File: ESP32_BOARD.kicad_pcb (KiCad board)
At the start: 4 copper layers, 36 x 63 mm, 70 parts, among them IC1 AP2112K-3.3, IC2 MPQ4420HGJ-Z, IC3 W25Q128JVSIQ, IC4 ESP32-S3R8, IC5 AW9364DNR, Q1 40MHz, SW1 TS-1010B-B-A, SW2 PTS810SJK250SMTRLFS, SW3 PTS810SJK250SMTRLFS

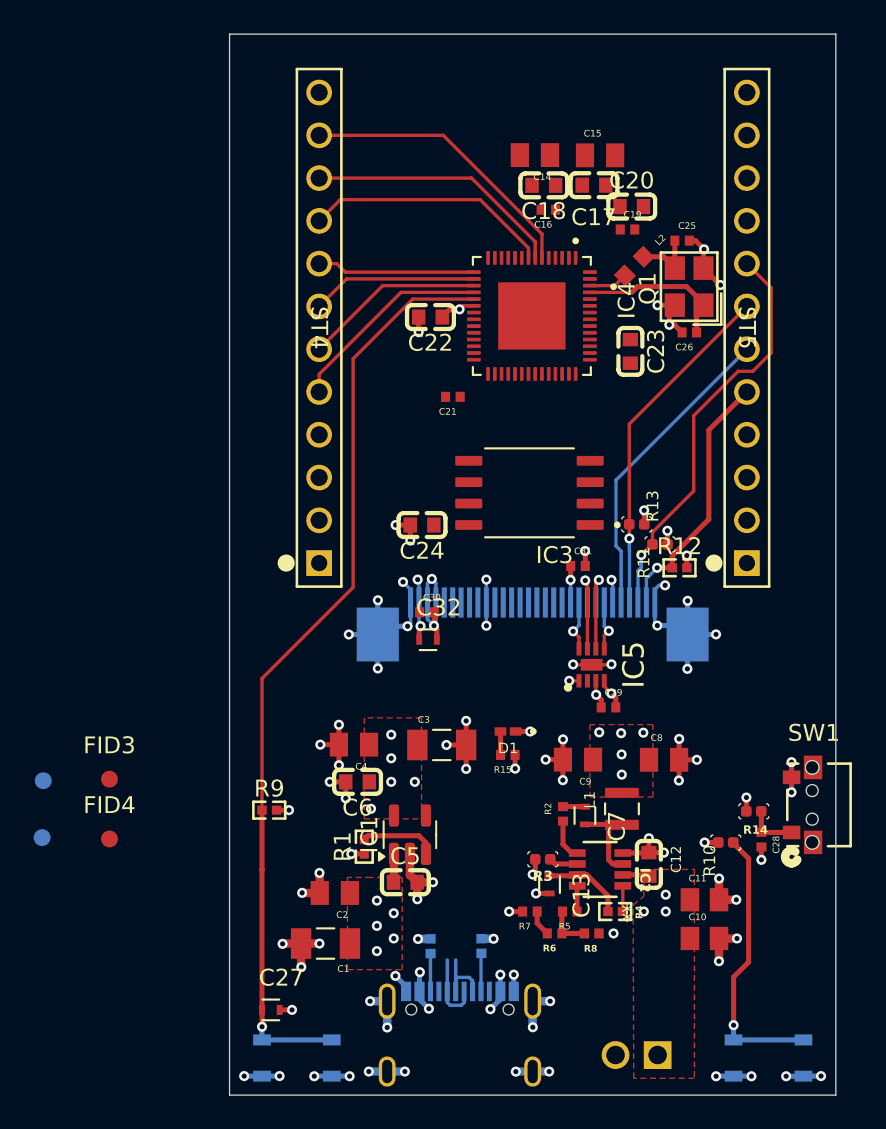
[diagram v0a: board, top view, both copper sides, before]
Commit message: Routing done | First Iteration
Silkscreen of components kinda done
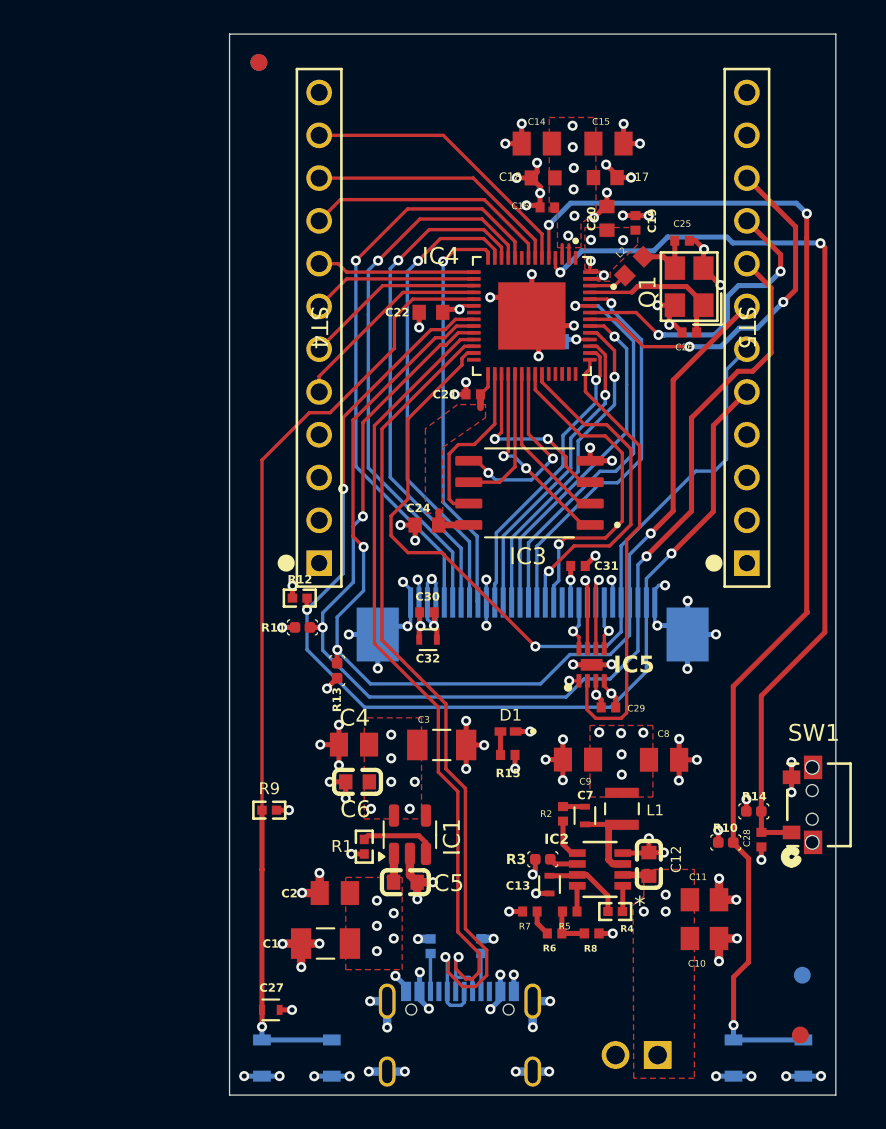
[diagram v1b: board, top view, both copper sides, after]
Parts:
- C23: moved to B.Cu
- moved FID4 47.0 mm to (79.1, 92.9)
- moved FID2 45.9 mm to (111.4, 147.1)
- moved FID1 44.5 mm to (79.1, 92.9)
- moved FID3 43.7 mm to (111.3, 150.6)
- moved R12 22.6 mm to (81.6, 124.7), turned to 180 degrees
- moved R11 21.8 mm to (81.7, 126.4), turned to 90 degrees
- moved R13 19.8 mm to (83.8, 129.0), turned to 0 degrees
- moved C23 4.79 mm to (96.5, 109.5), turned to 180 degrees
- moved C20 1.63 mm to (99.8, 102.1), turned to 90 degrees
- moved C21 1.22 mm to (91.9, 112.6)
- moved C15 0.86 mm to (99.9, 97.7)
- moved C17 0.81 mm to (99.7, 99.7)
- moved C14 0.69 mm to (95.6, 97.7)
- moved C19 0.61 mm to (101.5, 102.4), turned to 90 degrees
- moved C18 0.44 mm to (96.0, 99.7)
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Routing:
- net GPIO0: track 16.6 -> 73.9 mm, vias 1 -> 3
- net RESET: track 3.04 -> 55.9 mm, vias 0 -> 2
- net ESP_TP_INT: track 15.5 -> 67.1 mm, vias 1 -> 3
- net I2C_SDA: track 24.5 -> 72.5 mm, vias 1 -> 3
- net ESP_USB_D+: track 4.33 -> 51.0 mm, vias 0 -> 1
- net I2C_SCL: track 20.5 -> 66.7 mm, vias 1 -> 3
- net ESP_USB_D-: track 4.41 -> 50.3 mm, vias 0 -> 1
- net ESP_LCD_RES: track 0.00 -> 35.0 mm, vias 0 -> 1
- net ESP_LCD_CS: track 0.00 -> 32.8 mm, vias 0 -> 1
- net ESP_TP_RESET: track 18.4 -> 50.4 mm, vias 0 -> 1
- net ESP_LCD_D/C: track 0.00 -> 30.2 mm, vias 0 -> 1
- net GND: track 108.8 -> 136.8 mm, vias 81 -> 102
- net ESP_LCD_WR: track 0.00 -> 27.9 mm, vias 0 -> 1
- net ESP_LCD_BLK: track 0.00 -> 27.2 mm
- net ESP_LCD_RD: track 0.00 -> 24.5 mm, vias 0 -> 1
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- added copper zone on F.Cu, net VDD_SDIO

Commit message: Minor adjustments to the layout and the silkscreen
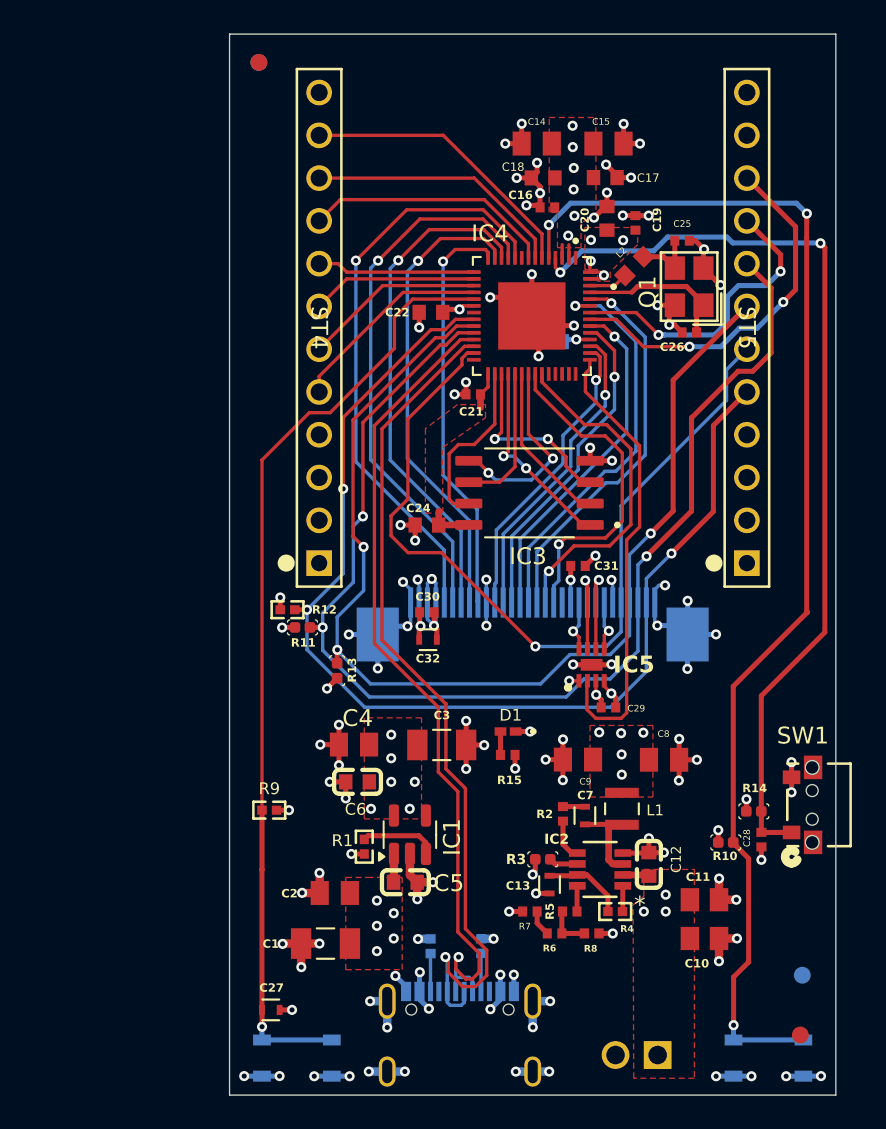
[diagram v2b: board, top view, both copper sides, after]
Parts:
- moved R12 1.00 mm to (80.8, 125.4)
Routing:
- net ESP_TP_RESET: track 50.4 -> 49.7 mm

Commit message: Layout ready for export
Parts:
- moved R8 0.24 mm to (98.7, 144.5)
- moved R6 0.14 mm to (96.7, 144.5)
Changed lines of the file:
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@@
 	(footprint "RC0402FR-0733KL:RESC1005X40N"
 		(layer "F.Cu")
-		(at 96.7 144.6 180)
+		(at 96.725 144.46 180)
 		(property "Reference" "R6"
 			(at 0.3 -0.88 0)
@@
 	(footprint "0402WGF1302TCE:RESC1005X40N"
 		(layer "F.Cu")
-		(at 98.9 144.6)
+		(at 98.7 144.46)
 		(property "Reference" "R8"
 			(at -0.06 0.9 0)
@@
 	)
 	(segment
-		(start 97.132 144.6)
-		(end 97.132 143.336)
+		(start 97.157 144.46)
+		(end 98.265 144.46)
 		(width 0.3)
 		(layer "F.Cu")
@@
 	)
 	(segment
-		(start 97.132 144.6)
-		(end 98.465 144.6)
+		(start 97.168 143.3)
+		(end 97.168 144.449)
 		(width 0.3)
 		(layer "F.Cu")
@@
 	)
 	(segment
-		(start 97.132 143.336)
-		(end 97.168 143.3)
+		(start 97.168 144.449)
+		(end 97.157 144.46)
 		(width 0.3)
 		(layer "F.Cu")
@@
 	)
 	(segment
-		(start 96.268 144.6)
-		(end 95.664 143.996)
+		(start 95.664 143.831)
+		(end 96.293 144.46)
 		(width 0.3)
 		(layer "F.Cu")
@@
 	)
 	(segment
-		(start 95.664 143.996)
-		(end 95.664 143.3)
+		(start 95.664 143.3)
+		(end 95.664 143.831)
 		(width 0.3)
 		(layer "F.Cu")
@@
 	)
 	(segment
-		(start 100.151429 144.6)
-		(end 100.154827 144.603398)
+		(start 99.951429 144.46)
+		(end 99.954827 144.463398)
 		(width 0.3)
 		(layer "F.Cu")
@@
 	)
 	(segment
-		(start 99.335 144.6)
-		(end 100.151429 144.6)
+		(start 99.135 144.46)
+		(end 99.951429 144.46)
 		(width 0.3)
 		(layer "F.Cu")
@@
 	)
 	(via
-		(at 100.154827 144.603398)
+		(at 99.954827 144.463398)
 		(size 0.6)
 		(drill 0.3)
@@
 	)
 	(segment
-		(start 89.92 109.66)
-		(end 85.32 114.26)
-		(width 0.2)
-		(layer "F.Cu")
-		(net 27)
-	)
-	(segment
-		(start 90.975 108.935)
-		(end 90.25 109.66)
+		(start 90.28 109.66)
+		(end 89.92 109.66)
 		(width 0.2)
 		(layer "F.Cu")
@@
 	)
 	(segment
+		(start 91.905 108.935)
+		(end 91.005 108.935)
+		(width 0.2)
+		(layer "F.Cu")
+		(net 27)
+	)
+	(segment
+		(start 91.005 108.935)
+		(end 90.28 109.66)
+		(width 0.2)
+		(layer "F.Cu")
+		(net 27)
+	)
+	(segment
 		(start 109.56 110.13)
 		(end 109.56 106.2701)
@@
 	)
 	(segment
-		(start 85.32 114.26)
-		(end 85.32 119.84)
+		(start 89.92 109.66)
+		(end 85.32 114.26)
 		(width 0.2)
 		(layer "F.Cu")
@@
 	)
 	(segment
-		(start 91.905 108.935)
-		(end 90.975 108.935)
-		(width 0.2)
+		(start 102.16 122.19)
+		(end 104.83 119.52)
+		(width 0.3)
 		(layer "F.Cu")
 		(net 27)
 	)
 	(segment
-		(start 90.25 109.66)
-		(end 89.92 109.66)
+		(start 85.32 114.26)
+		(end 85.32 119.84)
 		(width 0.2)
 		(layer "F.Cu")
@@
 	)
 	(segment
-		(start 102.16 122.19)
-		(end 104.83 119.52)
-		(width 0.3)
-		(layer "F.Cu")
-		(net 27)
-	)
-	(segment
 		(start 102.16 122.21)
 		(end 102.16 122.19)
@@
 	)
 	(segment
-		(start 84.73 121.02)
-		(end 85.36 121.65)
-		(width 0.2)
-		(layer "F.Cu")
-		(net 37)
-	)
-	(segment
 		(start 103.74 111.7499)
 		(end 103.74 119.52)
@@
 	)
 	(segment
-		(start 90.18 109.23)
-		(end 89.625678 109.23)
+		(start 84.73 114.125678)
+		(end 84.73 121.02)
 		(width 0.2)
 		(layer "F.Cu")
@@
 	)
 	(segment
-		(start 91.905 108.535)
-		(end 90.875 108.535)
-		(width 0.2)
+		(start 103.74 119.52)
+		(end 102.41 120.85)
+		(width 0.3)
 		(layer "F.Cu")
 		(net 37)
 	)
 	(segment
-		(start 84.73 114.125678)
-		(end 84.73 121.02)
-		(width 0.2)
+		(start 108.1199 107.37)
+		(end 103.74 111.7499)
+		(width 0.3)
 		(layer "F.Cu")
 		(net 37)
 	)
 	(segment
-		(start 103.74 119.52)
-		(end 102.41 120.85)
-		(width 0.3)
+		(start 89.625678 109.23)
+		(end 84.73 114.125678)
+		(width 0.2)
 		(layer "F.Cu")
 		(net 37)
 	)
 	(segment
-		(start 90.875 108.535)
-		(end 90.18 109.23)
+		(start 90.21 109.23)
+		(end 89.625678 109.23)
 		(width 0.2)
 		(layer "F.Cu")
@@
 	)
 	(segment
-		(start 108.1199 107.37)
-		(end 103.74 111.7499)
-		(width 0.3)
+		(start 91.905 108.535)
+		(end 90.905 108.535)
+		(width 0.2)
 		(layer "F.Cu")
 		(net 37)
@@
 	)
 	(segment
-		(start 89.625678 109.23)
-		(end 84.73 114.125678)
+		(start 84.73 121.02)
+		(end 85.36 121.65)
+		(width 0.2)
+		(layer "F.Cu")
+		(net 37)
+	)
+	(segment
+		(start 90.905 108.535)
+		(end 90.21 109.23)
 		(width 0.2)
 		(layer "F.Cu")
@@
 		(polygon
 			(pts
-				(xy 92.6 113.2) (xy 90.933334 113.2) (xy 89.03 114.6275) (xy 89.03 119.64) (xy 90.06 119.64) (xy 90.06 115.743024)
-				(xy 92.6 113.976067)
+				(xy 92.6 113.2) (xy 90.933334 113.2) (xy 89.03 114.6275) (xy 89.03 119.64) (xy 90.04 119.64) (xy 90.04 115.739979)
+				(xy 92.6 113.959109)
 			)
 		)

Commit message: Finished Layout | Ver. 1.0
Layout finished for ver. 1.0

Design at a stage before the review from the colleagues
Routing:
- net GND: track 136.8 -> 139.8 mm, vias 102 -> 103
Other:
- board text added: "12V"
- board text added: "3V3"
- board text added: "Boris Ivanov"
- board text added: "GND"
- board text added: "GPIO1"
- board text added: "GPIO10"
- board text added: "GPIO11"
- board text added: "GPIO12"
- board text added: "GPIO13"
- board text added: "GPIO2"
- board text added: "GPIO3"
- board text added: "TU - Sofia"
- board text added: "U0RXD"
- board text added: "U0TXD"
